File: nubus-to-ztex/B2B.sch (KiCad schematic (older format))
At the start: 13 parts, among them J1 Conn_02x07_Odd_Even, J3 Conn_01x06_Male

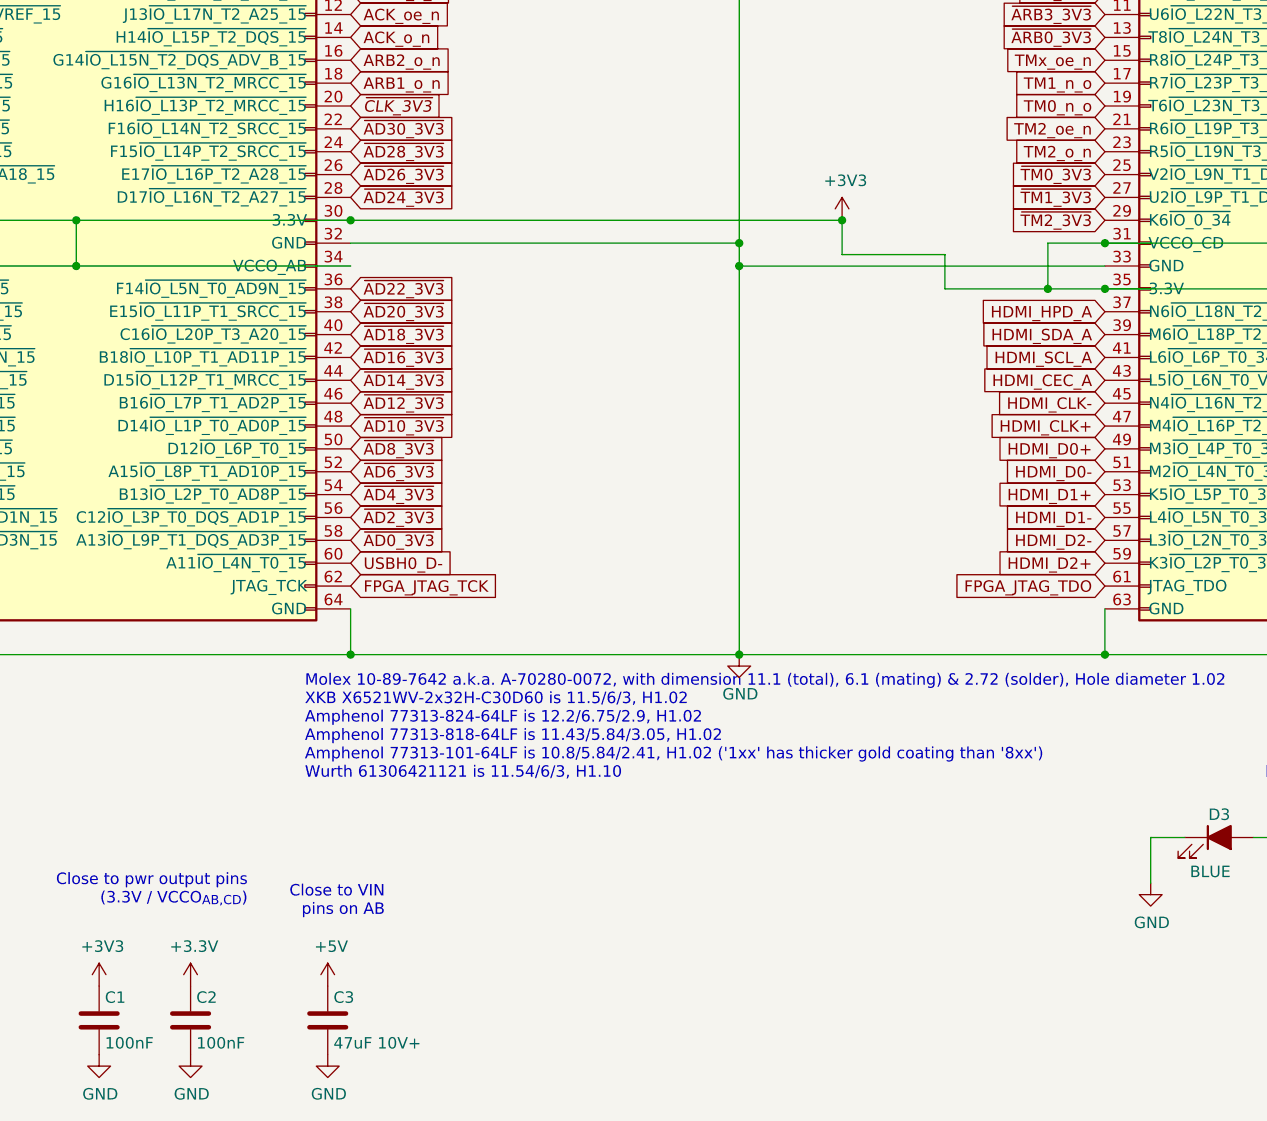
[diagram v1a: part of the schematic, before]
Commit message: move shielding to hdmi, trace cleanup
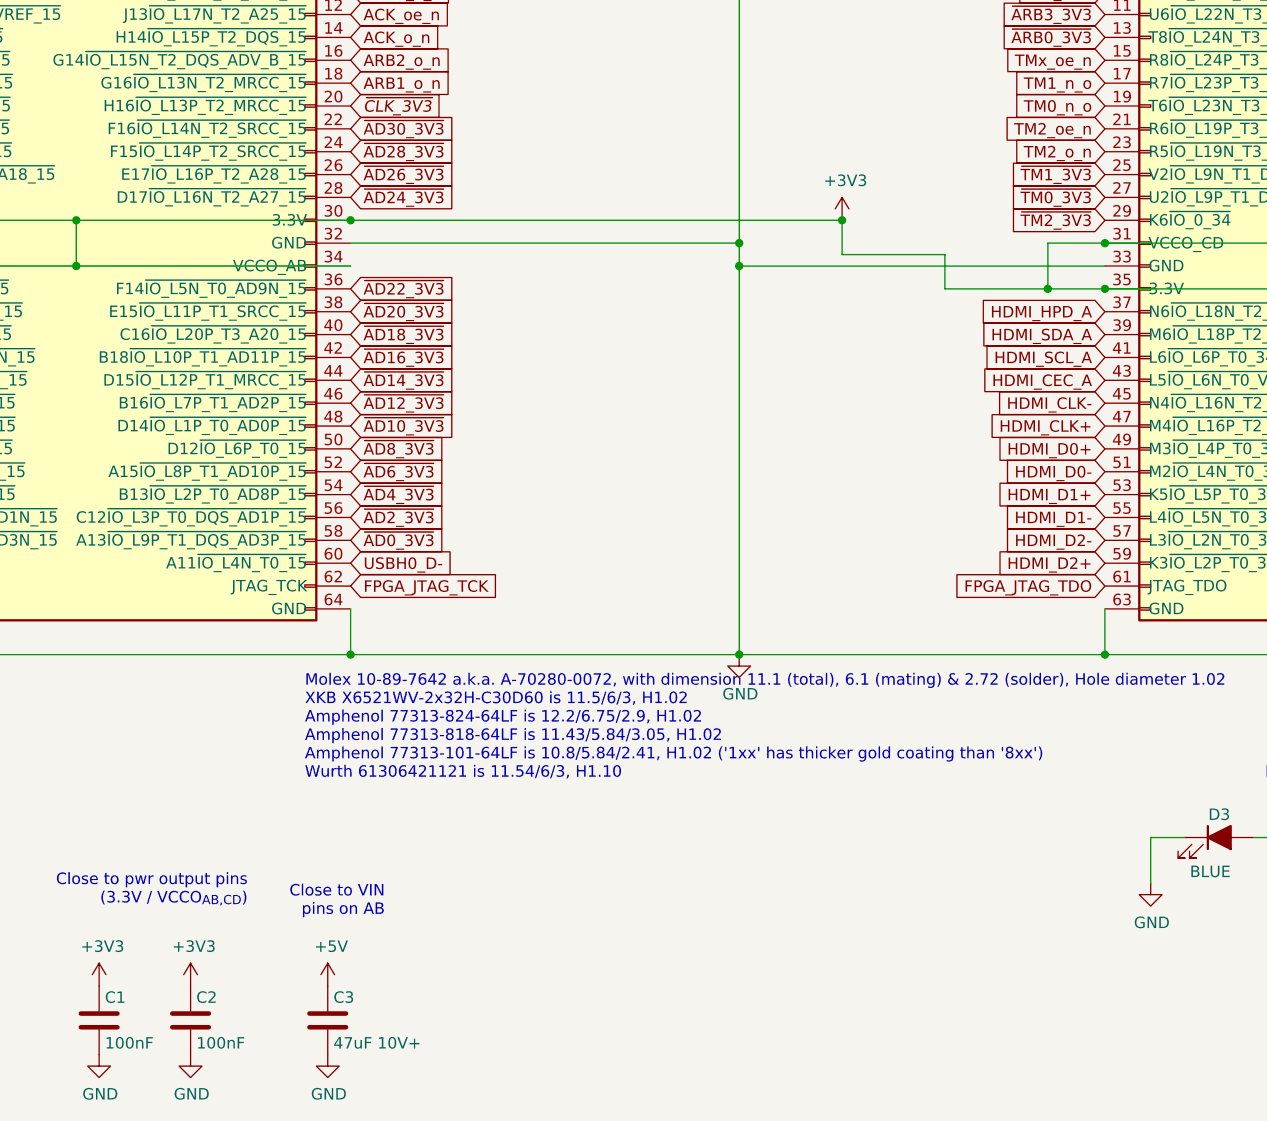
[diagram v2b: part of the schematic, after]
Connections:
- net ~TM0_3V3: now also JCD1.27 (U2~IO_L9P_T1_DQS_34); no longer JCD1.25 (V2~IO_L9N_T1_DQS_34)
- net ~TM1_3V3: now also JCD1.25 (V2~IO_L9N_T1_DQS_34); no longer JCD1.27 (U2~IO_L9P_T1_DQS_34)
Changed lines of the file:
@@
 $Descr A4 11693 8268
 encoding utf-8
-Sheet 2 9
+Sheet 2 8
 Title "nubus-to-ztex B2B connector"
 Date ""
@@
 Text GLabel 9900 2550 2    50   Input ~ 0
 ~RESET_3V3
+Text GLabel 7400 2350 0    50   Input ~ 0
+~TM1_3V3
 Text GLabel 7400 2450 0    50   Input ~ 0
-~TM1_3V3
-Text GLabel 7400 2350 0    50   Input ~ 0
 ~TM0_3V3
 Text GLabel 1600 3950 0    50   Input ~ 0
@@
 F 3 "" H 3400 6200 50  0001 C CNN
 	1    3400 6200
-	1    0    0    -1
-$EndComp
-$Comp
-L power:+3.3V #PWR08
-U 1 1 61F0853E
-P 3400 5900
-F 0 "#PWR08" H 3400 5750 50  0001 C CNN
-F 1 "+3.3V" H 3415 6073 50  0000 C CNN
-F 2 "" H 3400 5900 50  0001 C CNN
-F 3 "" H 3400 5900 50  0001 C CNN
-	1    3400 5900
 	1    0    0    -1
 $EndComp
@@
 Text GLabel 9900 2950 2    50   Input ~ 0
 PMOD-15
+$Comp
+L power:+3V3 #PWR0110
+U 1 1 6343D117
+P 3400 5900
+F 0 "#PWR0110" H 3400 5750 50  0001 C CNN
+F 1 "+3V3" H 3415 6073 50  0000 C CNN
+F 2 "" H 3400 5900 50  0001 C CNN
+F 3 "" H 3400 5900 50  0001 C CNN
+	1    3400 5900
+	1    0    0    -1
+$EndComp
 $EndSCHEMATC

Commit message: update everything
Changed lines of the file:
@@
 EESchema Schematic File Version 4
-LIBS:nubus-to-ztex-cache
-EELAYER 26 0
+EELAYER 30 0
 EELAYER END
 $Descr A4 11693 8268
@@
 Wire Wire Line
 	10200 1350 9900 1350
-Wire Wire Line
-	9450 1050 10200 1050
 Text GLabel 4100 2050 2    50   Input Italic 0
 ~CLK_3V3
@@
 Text GLabel 1850 6400 2    60   Input ~ 12
 LED1
-Text GLabel 9450 1050 2    60   Input ~ 12
+Text GLabel 9650 1050 2    60   Input ~ 12
 LED0
-Text GLabel 9450 950  2    60   Input ~ 12
+Text GLabel 9650 950  2    60   Input ~ 12
 LED1
 Text GLabel 1600 4050 0    50   Input ~ 0
@@
 	1    0    0    -1
 $EndComp
+Wire Wire Line
+	9450 950  9650 950
+Connection ~ 9450 950
+Wire Wire Line
+	9450 1050 10200 1050
 $EndSCHEMATC

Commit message: more JTAG from TH to SMD
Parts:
- J1: footprint For_SeeedStudio:PinHeader_2x07_P2.00mm_Vertical_For_SeeedStudio -> For_SeeedStudio:MOLEX_87832-1420; Datasheet-ALT https://datasheet.lcsc.com/lcsc/1811051309_MOLEX-878311420_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 -> (none); MPN 87831-1420 -> 87832-1420; MPN Right Angle 87833-1420 -> (none); MPN-ALT Right Angle A2005WR-N-2X7P-B -> (none); Notes 87831-1419, 87831-1420, 87831-1421, 87831-1436 only change 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 -> (none); URL https://www2.mouser.com/ProductDetail/Molex/87831-1420?qs=Q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 -> https://www.mouser.fr/ProductDetail/Molex/87832-1420?qs=9Wl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; URL Rihgt Angle https://www2.mouser.com/ProductDetail/Molex/87833-1420?qs=%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 -> (none)
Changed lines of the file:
@@
 F 0 "J1" H 3200 7767 50  0000 C CNN
 F 1 "Conn_02x07_Odd_Even" H 3200 7676 50  0000 C CNN
-F 2 "For_SeeedStudio:PinHeader_2x07_P2.00mm_Vertical_For_SeeedStudio" H 3150 7250 50  0001 C CNN
+F 2 "For_SeeedStudio:MOLEX_87832-1420" H 3150 7250 50  0001 C CNN
 F 3 "https://www.molex.com/pdm_docs/sd/878331420_sd.pdf" H 3150 7250 50  0001 C CNN
-F 4 "87833-1420" H 3150 7250 50  0001 C CNN "MPN Right Angle"
-F 5 "A2005WR-N-2X7P-B" H 3150 7250 50  0001 C CNN "MPN-ALT Right Angle"
-F 6 "https://www2.mouser.com/ProductDetail/Molex/87833-1420?qs=%2Fha2pyFadujYFYCIYI1IvFCvLi7no9WQYzIL%2FpYxKhg%3D" H 3150 7250 50  0001 C CNN "URL Rihgt Angle"
-F 7 "87831-1420" H 3150 7250 50  0001 C CNN "MPN"
-F 8 "https://www2.mouser.com/ProductDetail/Molex/87831-1420?qs=QtQX4uD3c2VDCL534TqpVg%3D%3D" H 3150 7250 50  0001 C CNN "URL"
-F 9 "https://datasheet.lcsc.com/lcsc/1811051309_MOLEX-878311420_C240854.pdf" H 3150 7250 50  0001 C CNN "Datasheet-ALT"
-F 10 "87831-1419, 87831-1420, 87831-1421, 87831-1436 only change plating" H 3150 7250 50  0001 C CNN "Notes"
+F 4 "87832-1420" H 3150 7250 50  0001 C CNN "MPN"
+F 5 "https://www.mouser.fr/ProductDetail/Molex/87832-1420?qs=9Wl4wMk6Njp2JciwISLQUQ%3D%3D" H 3150 7250 50  0001 C CNN "URL"
 	1    3150 7250
 	1    0    0    -1

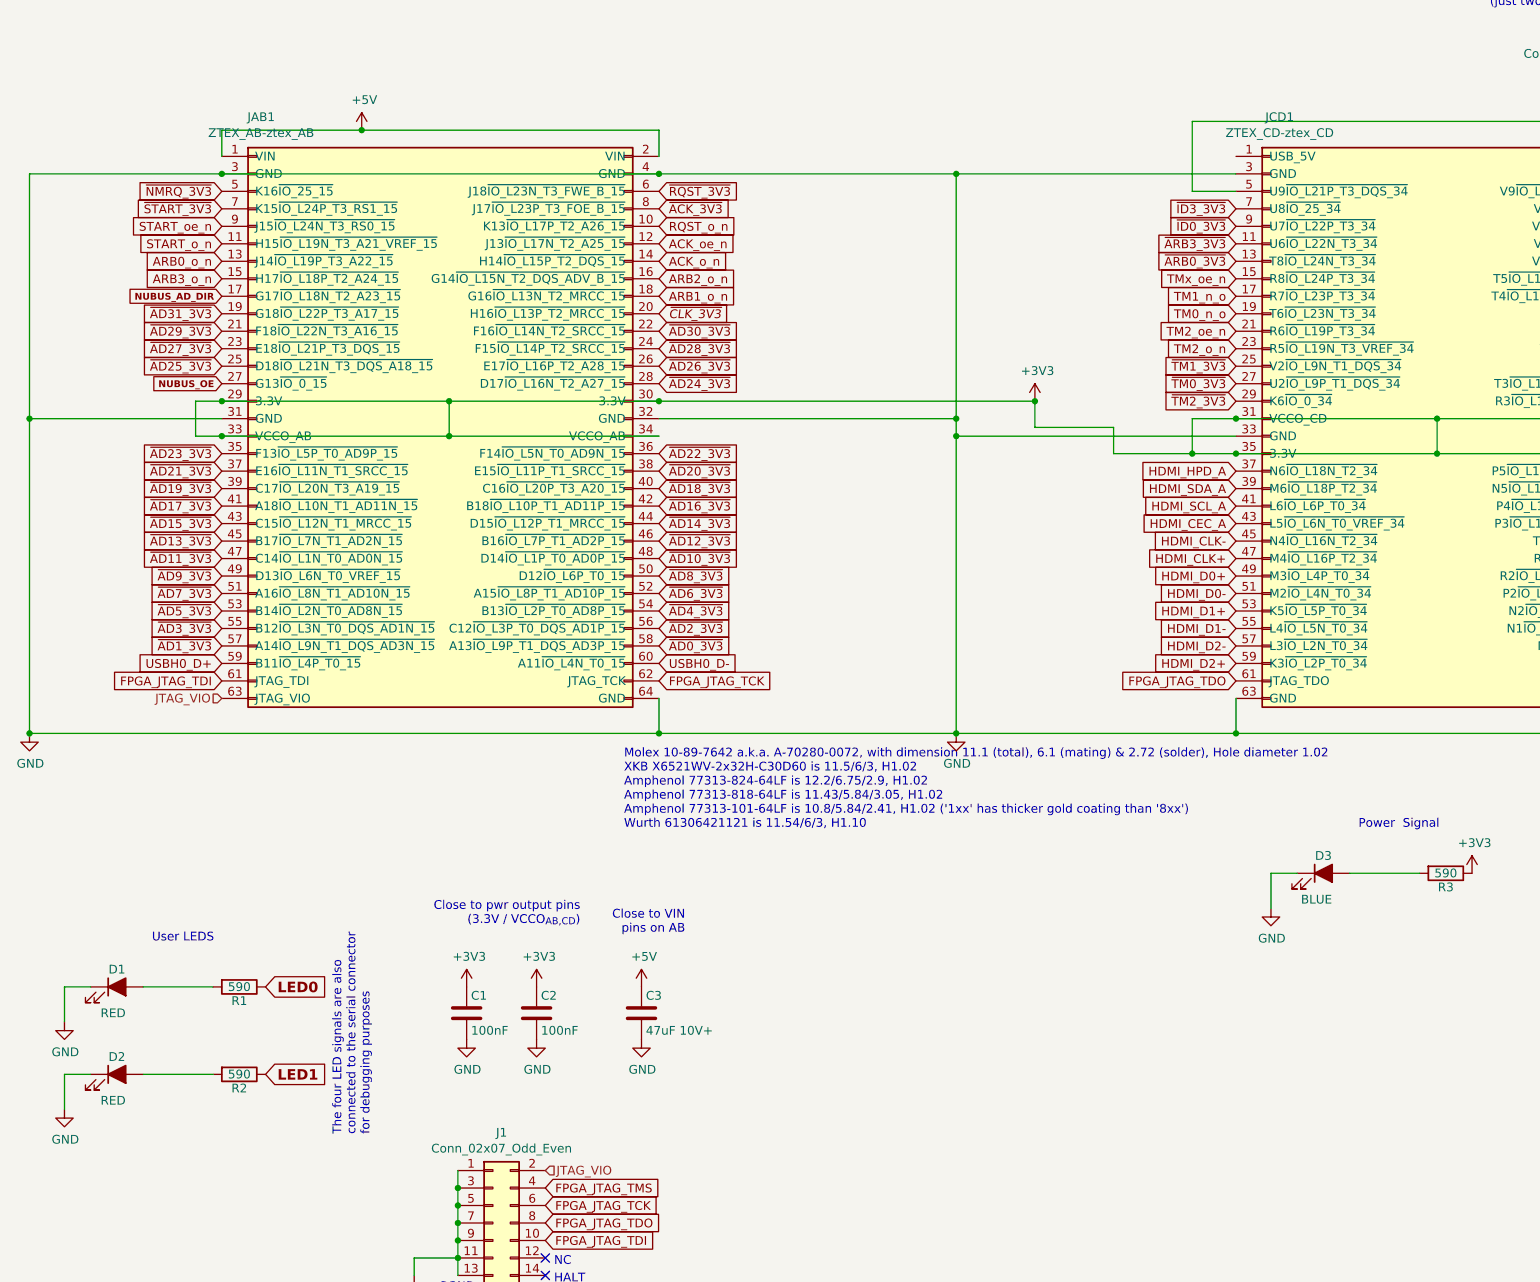
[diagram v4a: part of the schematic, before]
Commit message: more update to V1.2 to try to limit cost
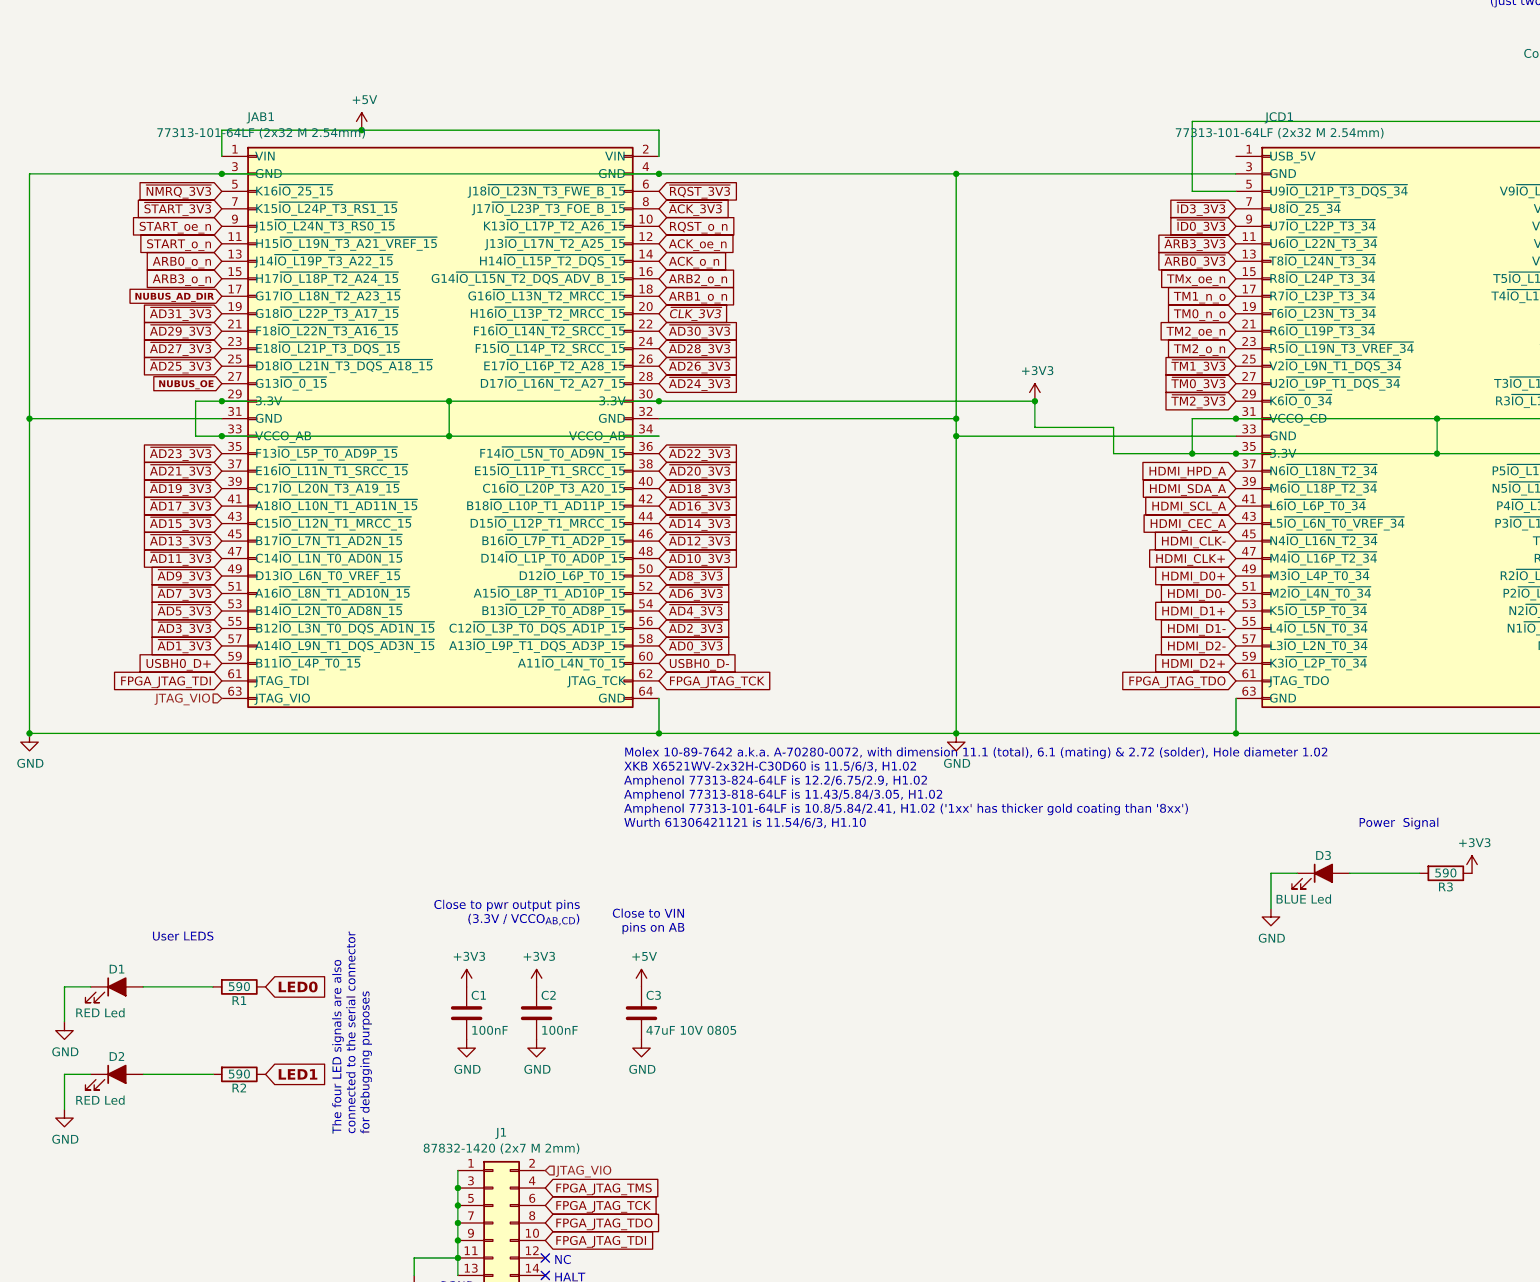
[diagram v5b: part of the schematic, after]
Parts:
- C3: value 47uF 10V+ -> 47uF 10V 0805
- D1, D2: value RED -> RED Led
- D3: value BLUE -> BLUE Led
- J1: value Conn_02x07_Odd_Even -> 87832-1420 (2x7 M 2mm)
- JAB1: value ZTEX_AB-ztex_AB -> 77313-101-64LF (2x32 M 2.54mm)
- JCD1: value ZTEX_CD-ztex_CD -> 77313-101-64LF (2x32 M 2.54mm)
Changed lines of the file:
@@
 AR Path="/618E8C75/5F676E85" Ref="JAB1"  Part="1"
 F 0 "JAB1" H 1825 4375 50  0000 C CNN
-F 1 "ZTEX_AB-ztex_AB" H 1825 4284 50  0000 C CNN
+F 1 "77313-101-64LF (2x32 M 2.54mm)" H 1825 4284 50  0000 C CNN
 F 2 "For_SeeedStudio:PinHeader_2x32_P2.54mm_Vertical_For_SeeedStudio" H 1800 2650 50  0001 C CNN
 F 3 "" H 1800 2650 50  0001 C CNN
@@
 AR Path="/618E8C75/5F676F65" Ref="JCD1"  Part="1"
 F 0 "JCD1" H 7650 4375 50  0000 C CNN
-F 1 "ZTEX_CD-ztex_CD" H 7650 4284 50  0000 C CNN
+F 1 "77313-101-64LF (2x32 M 2.54mm)" H 7650 4284 50  0000 C CNN
 F 2 "For_SeeedStudio:PinHeader_2x32_P2.54mm_Vertical_For_SeeedStudio" H 7600 2650 50  0001 C CNN
 F 3 "" H 7600 2650 50  0001 C CNN
@@
 P 3150 7250
 F 0 "J1" H 3200 7767 50  0000 C CNN
-F 1 "Conn_02x07_Odd_Even" H 3200 7676 50  0000 C CNN
+F 1 "87832-1420 (2x7 M 2mm)" H 3200 7676 50  0000 C CNN
 F 2 "For_SeeedStudio:MOLEX_87832-1420" H 3150 7250 50  0001 C CNN
 F 3 "https://www.molex.com/pdm_docs/sd/878331420_sd.pdf" H 3150 7250 50  0001 C CNN
@@
 AR Path="/618E8C75/61B5DFCC" Ref="D1"  Part="1"
 F 0 "D1" H 1000 6000 50  0000 C CNN
-F 1 "RED" H 1050 5750 50  0000 R CNN
+F 1 "RED Led" H 1050 5750 50  0000 R CNN
 F 2 "LED_SMD:LED_0805_2012Metric" H 1000 5900 50  0001 C CNN
 F 3 "https://optoelectronics.liteon.com/upload/download/DS-22-99-0150/LTST-C170KRKT.pdf" H 1000 5900 50  0001 C CNN
@@
 AR Path="/618E8C75/61B5F405" Ref="D2"  Part="1"
 F 0 "D2" H 1000 6500 50  0000 C CNN
-F 1 "RED" H 1050 6250 50  0000 R CNN
+F 1 "RED Led" H 1050 6250 50  0000 R CNN
 F 2 "LED_SMD:LED_0805_2012Metric" H 1000 6400 50  0001 C CNN
 F 3 "https://optoelectronics.liteon.com/upload/download/DS-22-99-0150/LTST-C170KRKT.pdf" H 1000 6400 50  0001 C CNN
@@
 AR Path="/618E8C75/621E3C57" Ref="D3"  Part="1"
 F 0 "D3" H 7900 5350 50  0000 C CNN
-F 1 "BLUE" H 7950 5100 50  0000 R CNN
+F 1 "BLUE Led" H 7950 5100 50  0000 R CNN
 F 2 "LED_SMD:LED_0805_2012Metric" H 7900 5250 50  0001 C CNN
 F 3 "https://eu.mouser.com/datasheet/2/239/Lite-On-LTST-C170TBKT-1175372.pdf" H 7900 5250 50  0001 C CNN
@@
 AR Path="/618E8C75/621FCA7B" Ref="C3"  Part="1"
 F 0 "C3" H 4025 6150 50  0000 L CNN
-F 1 "47uF 10V+" H 4025 5950 50  0000 L CNN
+F 1 "47uF 10V 0805" H 4025 5950 50  0000 L CNN
 F 2 "Capacitor_SMD:C_0805_2012Metric" H 4038 5900 50  0001 C CNN
 F 3 "" H 4000 6050 50  0000 C CNN
